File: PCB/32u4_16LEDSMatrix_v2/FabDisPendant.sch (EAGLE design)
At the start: 55 parts, among them IC1 MPR121, U1 ATMEGA32U4-AU, Y1 16MHz

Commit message: Finished PCB v2 basics
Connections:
- removed net D13: U1.PC7
- removed net D5: U1.PC6
- new net D10: U1.PB6
- new net D9: U1.PB5
- net LEDS_CI: now also U1.PC7; no longer U1.PB5
- net LEDS_DI: now also U1.PC6; no longer U1.PB6
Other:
- moved on the sheet: C20
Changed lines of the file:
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@@
 <instance part="GND35" gate="1" x="88.9" y="170.18"/>
 <instance part="R2" gate="G$1" x="154.94" y="177.8" rot="R270"/>
-<instance part="C20" gate="G$1" x="162.56" y="193.04" smashed="yes">
-<attribute name="NAME" x="161.544" y="192.913" size="1.778" layer="95" rot="R180"/>
-<attribute name="VALUE" x="161.544" y="197.739" size="1.778" layer="96" rot="R180"/>
-</instance>
-<instance part="GND37" gate="1" x="162.56" y="203.2" rot="R180"/>
+<instance part="C20" gate="G$1" x="165.1" y="193.04" smashed="yes">
+<attribute name="NAME" x="164.084" y="192.913" size="1.778" layer="95" rot="R180"/>
+<attribute name="VALUE" x="164.084" y="197.739" size="1.778" layer="96" rot="R180"/>
+</instance>
+<instance part="GND37" gate="1" x="165.1" y="203.2" rot="R180"/>
 <instance part="P+11" gate="G$1" x="154.94" y="167.64" smashed="yes" rot="R180">
 <attribute name="VALUE" x="157.226" y="164.338" size="1.778" layer="96" rot="R180"/>
@@
 <attribute name="VALUE" x="175.514" y="213.868" size="1.778" layer="96"/>
 </instance>
-<instance part="USBVCC2" gate="G$1" x="167.64" y="205.74"/>
+<instance part="USBVCC2" gate="G$1" x="168.91" y="205.74"/>
 <instance part="GND39" gate="1" x="187.96" y="139.7"/>
 <instance part="GND53" gate="1" x="241.3" y="157.48" rot="R90"/>
@@
 </segment>
 <segment>
-<wire x1="162.56" y1="200.66" x2="162.56" y2="198.12" width="0.1524" layer="91"/>
+<wire x1="165.1" y1="200.66" x2="165.1" y2="198.12" width="0.1524" layer="91"/>
 <pinref part="C20" gate="G$1" pin="1"/>
 <pinref part="GND37" gate="1" pin="GND"/>
@@
 </segment>
 <segment>
-<wire x1="60.96" y1="218.44" x2="76.2" y2="218.44" width="0.1524" layer="91"/>
-<wire x1="76.2" y1="198.12" x2="76.2" y2="218.44" width="0.1524" layer="91"/>
-<pinref part="F1" gate="G$1" pin="2"/>
-<label x="64.77" y="218.44" size="1.778" layer="95"/>
-<wire x1="101.6" y1="203.2" x2="101.6" y2="218.44" width="0.1524" layer="91"/>
-<pinref part="7803-???" gate="A1" pin="VO"/>
-<wire x1="116.84" y1="218.44" x2="101.6" y2="218.44" width="0.1524" layer="91"/>
-<pinref part="C4" gate="G$1" pin="2"/>
-<wire x1="76.2" y1="218.44" x2="101.6" y2="218.44" width="0.1524" layer="91"/>
-<junction x="76.2" y="218.44"/>
-<junction x="101.6" y="218.44"/>
-<label x="106.68" y="218.44" size="1.778" layer="95"/>
-</segment>
-<segment>
 <pinref part="ISP" gate="G$1" pin="2"/>
 <pinref part="SUPPLY2" gate="G$1" pin="VCC"/>
@@
 <label x="72.136" y="198.374" size="1.778" layer="95"/>
 <pinref part="C3" gate="G$1" pin="2"/>
+<pinref part="F1" gate="G$1" pin="2"/>
+<label x="64.77" y="218.44" size="1.778" layer="95"/>
+<wire x1="101.6" y1="203.2" x2="101.6" y2="218.44" width="0.1524" layer="91"/>
+<pinref part="7803-???" gate="A1" pin="VO"/>
+<wire x1="116.84" y1="218.44" x2="101.6" y2="218.44" width="0.1524" layer="91"/>
+<pinref part="C4" gate="G$1" pin="2"/>
+<wire x1="60.96" y1="218.44" x2="76.2" y2="218.44" width="0.1524" layer="91"/>
+<junction x="101.6" y="218.44"/>
+<label x="106.68" y="218.44" size="1.778" layer="95"/>
+<wire x1="76.2" y1="218.44" x2="101.6" y2="218.44" width="0.1524" layer="91"/>
+<wire x1="76.2" y1="198.12" x2="76.2" y2="218.44" width="0.1524" layer="91"/>
+<junction x="76.2" y="218.44"/>
 </segment>
 <segment>
@@
 <pinref part="C20" gate="G$1" pin="2"/>
 <pinref part="U1" gate="A" pin="AREF"/>
-<wire x1="162.56" y1="190.5" x2="190.5" y2="190.5" width="0.1524" layer="91"/>
+<wire x1="165.1" y1="190.5" x2="190.5" y2="190.5" width="0.1524" layer="91"/>
 </segment>
 </net>
@@
 <wire x1="190.5" y1="187.96" x2="162.56" y2="187.96" width="0.1524" layer="91"/>
 <junction x="162.56" y="187.96"/>
+<label x="154.94" y="187.96" size="1.778" layer="95"/>
 </segment>
 <segment>
@@
 <wire x1="226.06" y1="170.18" x2="236.22" y2="170.18" width="0.1524" layer="91"/>
 <label x="231.14" y="170.18" size="1.778" layer="95"/>
-</segment>
-</net>
-<net name="D5" class="0">
-<segment>
-<pinref part="U1" gate="A" pin="PC6"/>
-<wire x1="226.06" y1="187.96" x2="236.22" y2="187.96" width="0.1524" layer="91"/>
-<label x="231.14" y="187.96" size="1.778" layer="95"/>
 </segment>
 </net>
@@
 <pinref part="U1" gate="A" pin="UVCC"/>
 <wire x1="190.5" y1="205.74" x2="185.42" y2="205.74" width="0.1524" layer="91"/>
-<wire x1="185.42" y1="205.74" x2="167.64" y2="205.74" width="0.1524" layer="91"/>
+<wire x1="185.42" y1="205.74" x2="168.91" y2="205.74" width="0.1524" layer="91"/>
 <wire x1="185.42" y1="180.34" x2="185.42" y2="205.74" width="0.1524" layer="91"/>
 <pinref part="USBVCC2" gate="G$1" pin="3.3V"/>
@@
 <wire x1="226.06" y1="165.1" x2="236.22" y2="165.1" width="0.1524" layer="91"/>
 <label x="231.14" y="165.1" size="1.778" layer="95"/>
-</segment>
-</net>
-<net name="D13" class="0">
-<segment>
-<pinref part="U1" gate="A" pin="PC7"/>
-<wire x1="226.06" y1="185.42" x2="236.22" y2="185.42" width="0.1524" layer="91"/>
-<label x="231.14" y="185.42" size="1.778" layer="95"/>
 </segment>
 </net>
@@
 </segment>
 <segment>
-<pinref part="U1" gate="A" pin="PB6"/>
-<wire x1="226.06" y1="195.58" x2="236.22" y2="195.58" width="0.1524" layer="91"/>
-<label x="231.14" y="195.58" size="1.778" layer="95"/>
+<pinref part="U1" gate="A" pin="PC6"/>
+<wire x1="226.06" y1="187.96" x2="236.22" y2="187.96" width="0.1524" layer="91"/>
+<label x="231.14" y="187.96" size="1.778" layer="95"/>
 </segment>
 </net>
@@
 </segment>
 <segment>
-<pinref part="U1" gate="A" pin="PB5"/>
-<wire x1="226.06" y1="198.12" x2="236.22" y2="198.12" width="0.1524" layer="91"/>
-<label x="231.14" y="198.12" size="1.778" layer="95"/>
+<pinref part="U1" gate="A" pin="PC7"/>
+<wire x1="226.06" y1="185.42" x2="236.22" y2="185.42" width="0.1524" layer="91"/>
+<label x="231.14" y="185.42" size="1.778" layer="95"/>
 </segment>
 </net>
@@
 </segment>
 </net>
+<net name="D9" class="0">
+<segment>
+<pinref part="U1" gate="A" pin="PB5"/>
+<wire x1="226.06" y1="198.12" x2="236.22" y2="198.12" width="0.1524" layer="91"/>
+<label x="231.14" y="198.12" size="1.778" layer="95"/>
+</segment>
+</net>
+<net name="D10" class="0">
+<segment>
+<pinref part="U1" gate="A" pin="PB6"/>
+<wire x1="226.06" y1="195.58" x2="236.22" y2="195.58" width="0.1524" layer="91"/>
+<label x="231.14" y="195.58" size="1.778" layer="95"/>
+</segment>
+</net>

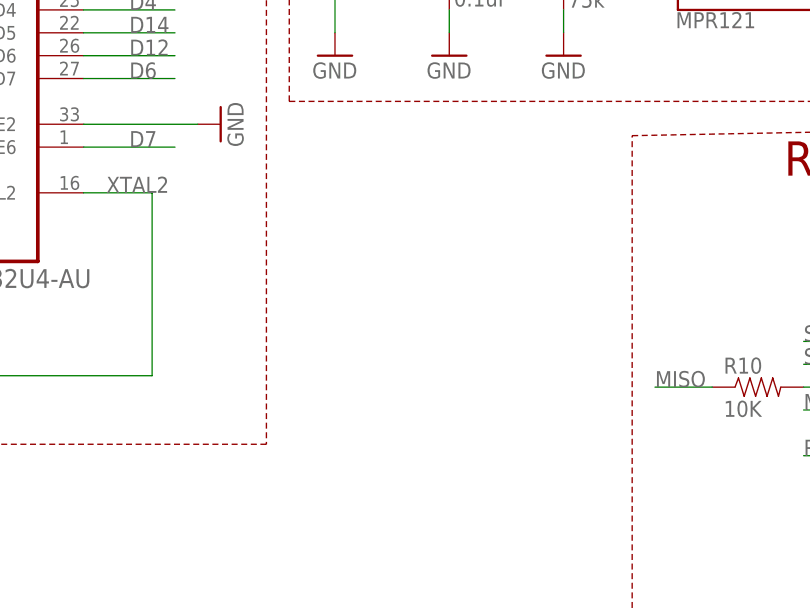
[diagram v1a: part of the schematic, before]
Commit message: Added headers for some digital and analog pins
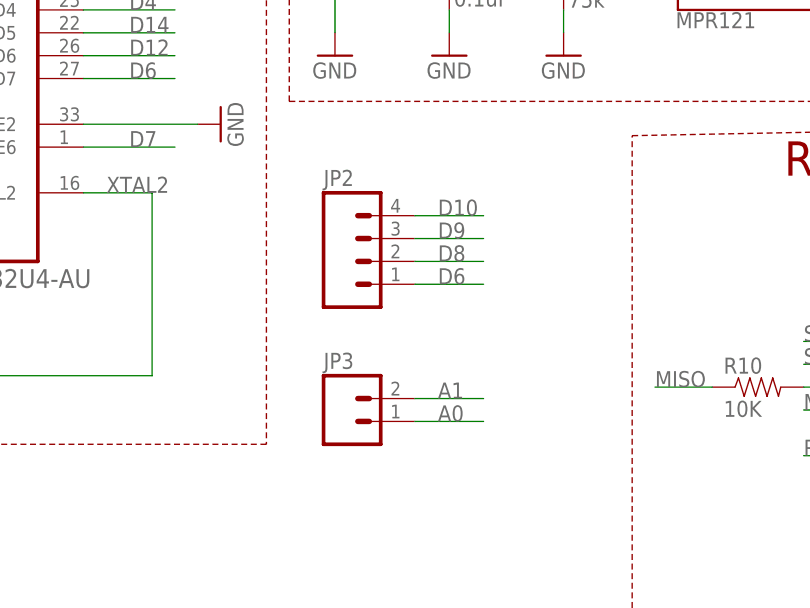
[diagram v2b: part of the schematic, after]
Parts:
- added JP2: (no value), SparkFun-Connectors:M04PTH
- added JP3: (no value), SparkFun-Connectors:M02PTH
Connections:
- net A0: now also JP3.1
- net A1: now also JP3.2
- net D10: now also JP2.4
- net D6: now also JP2.1
- net D8: now also JP2.2
- net D9: now also JP2.3
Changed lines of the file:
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@@
 <part name="PWRSWITCH" library="SparkFun" deviceset="SWITCH-MOMENTARY-2" device="SMD" value="Reset"/>
 <part name="JP1" library="SparkFun-Connectors" deviceset="M02" device="PTH"/>
+<part name="JP2" library="SparkFun-Connectors" deviceset="M04" device="PTH"/>
+<part name="JP3" library="SparkFun-Connectors" deviceset="M02" device="PTH"/>
 </parts>
 <sheets>
@@
 <instance part="PWRSWITCH" gate="G$1" x="55.88" y="166.37" rot="R180"/>
 <instance part="JP1" gate="G$1" x="314.96" y="245.11" rot="R180"/>
+<instance part="JP2" gate="G$1" x="257.81" y="142.24"/>
+<instance part="JP3" gate="G$1" x="255.27" y="124.46"/>
 </instances>
 <busses>
@@
 <label x="231.14" y="200.66" size="1.778" layer="95"/>
 </segment>
+<segment>
+<pinref part="JP2" gate="G$1" pin="2"/>
+<wire x1="262.89" y1="142.24" x2="270.51" y2="142.24" width="0.1524" layer="91"/>
+<label x="265.43" y="142.24" size="1.778" layer="95"/>
+</segment>
 </net>
 <net name="A5" class="0">
@@
 <label x="180.34" y="165.1" size="1.778" layer="95"/>
 </segment>
+<segment>
+<pinref part="JP3" gate="G$1" pin="2"/>
+<wire x1="262.89" y1="127" x2="270.51" y2="127" width="0.1524" layer="91"/>
+<label x="265.43" y="127" size="1.778" layer="95"/>
+</segment>
 </net>
 <net name="D4" class="0">
@@
 <wire x1="226.06" y1="162.56" x2="236.22" y2="162.56" width="0.1524" layer="91"/>
 <label x="231.14" y="162.56" size="1.778" layer="95"/>
+</segment>
+<segment>
+<pinref part="JP2" gate="G$1" pin="1"/>
+<wire x1="262.89" y1="139.7" x2="270.51" y2="139.7" width="0.1524" layer="91"/>
+<label x="265.43" y="139.7" size="1.778" layer="95"/>
 </segment>
 </net>
@@
 <label x="180.34" y="162.56" size="1.778" layer="95"/>
 </segment>
+<segment>
+<pinref part="JP3" gate="G$1" pin="1"/>
+<wire x1="262.89" y1="124.46" x2="270.51" y2="124.46" width="0.1524" layer="91"/>
+<label x="265.43" y="124.46" size="1.778" layer="95"/>
+</segment>
 </net>
 <net name="N$1" class="0">
@@
 <label x="231.14" y="198.12" size="1.778" layer="95"/>
 </segment>
+<segment>
+<pinref part="JP2" gate="G$1" pin="3"/>
+<wire x1="262.89" y1="144.78" x2="270.51" y2="144.78" width="0.1524" layer="91"/>
+<label x="265.43" y="144.78" size="1.778" layer="95"/>
+</segment>
 </net>
 <net name="D10" class="0">
@@
 <label x="231.14" y="195.58" size="1.778" layer="95"/>
 </segment>
-</net>
+<segment>
+<pinref part="JP2" gate="G$1" pin="4"/>
+<wire x1="262.89" y1="147.32" x2="270.51" y2="147.32" width="0.1524" layer="91"/>
+<label x="265.43" y="147.32" size="1.778" layer="95"/>
+</segment>
+</net>

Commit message: FInished up changes to the board
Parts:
- removed PWRSWITCH: Reset, SparkFun:SWITCH-MOMENTARY-2SMD
- added D2: (no value), SparkFun:DIODESOD
- added R12: 10k, SparkFun:RESISTOR0603-RES
- added SWITCH: SWITCH, SparkFun-Connectors:M03X2FEMALE
- R10: value 10K -> 4.7k
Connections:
- removed net D10: JP2.4, U1.PB6
- removed net D9: JP2.3, U1.PB5
- new net D13: JP2.4, U1.PC7
- new net D5: JP2.3, U1.PC6
- new net N$37: 7803-???.VO, C4.2, D2.C
- net 3.3V: now also R12.2
- net 5V: now also D2.A; no longer 7803-???.VO, C4.2
- net LEDS_CI: now also U1.PB6; no longer U1.PC7
- net LEDS_DI: now also U1.PB5; no longer U1.PC6
- net N$36: now also SWITCH.6; no longer PWRSWITCH.1
- net RAW: now also SWITCH.4; no longer PWRSWITCH.2
- net SS: now also R12.1
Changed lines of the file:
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@@
 <part name="GND16" library="SparkFun-Aesthetics" deviceset="GND" device=""/>
 <part name="LED15" library="APA102" deviceset="APA102" device=""/>
-<part name="R10" library="SparkFun" deviceset="RESISTOR" device="0603-RES" value="10K"/>
+<part name="R10" library="SparkFun" deviceset="RESISTOR" device="0603-RES" value="4.7k"/>
 <part name="C1" library="SparkFun-Capacitors" deviceset="10UF-6.3V-20%(1206)" device="" value="10uF"/>
 <part name="C2" library="SparkFun-Capacitors" deviceset="10UF-6.3V-20%(1206)" device="" value="10uF"/>
@@
 <part name="C4" library="SparkFun-Capacitors" deviceset="10UF-6.3V-20%(1206)" device="" value="10uF"/>
 <part name="C5" library="SparkFun-Capacitors" deviceset="10UF-6.3V-20%(1206)" device="" value="1uF"/>
-<part name="PWRSWITCH" library="SparkFun" deviceset="SWITCH-MOMENTARY-2" device="SMD" value="Reset"/>
 <part name="JP1" library="SparkFun-Connectors" deviceset="M02" device="PTH"/>
 <part name="JP2" library="SparkFun-Connectors" deviceset="M04" device="PTH"/>
 <part name="JP3" library="SparkFun-Connectors" deviceset="M02" device="PTH"/>
+<part name="D2" library="SparkFun" deviceset="DIODE" device="SOD"/>
+<part name="R12" library="SparkFun" deviceset="RESISTOR" device="0603-RES" value="10k"/>
+<part name="SWITCH" library="SparkFun-Connectors" deviceset="M03X2" device="FEMALE" value="SWITCH"/>
 </parts>
 <sheets>
@@
 <wire x1="353.06" y1="101.6" x2="287.02" y2="101.6" width="0.1524" layer="94" style="shortdash"/>
 <wire x1="287.02" y1="101.6" x2="287.02" y2="156.21" width="0.1524" layer="94" style="shortdash"/>
-<text x="303.911" y="151.765" size="3.81" layer="94">Radio</text>
 <wire x1="248.92" y1="223.52" x2="353.06" y2="223.52" width="0.1524" layer="94" style="shortdash"/>
 <wire x1="353.06" y1="223.52" x2="353.06" y2="160.02" width="0.1524" layer="94" style="shortdash"/>
@@
 <wire x1="142.24" y1="121.92" x2="142.24" y2="223.52" width="0.1524" layer="94" style="shortdash"/>
 <text x="143.891" y="217.805" size="3.81" layer="94">ATMEGA 32u4</text>
+<text x="288.671" y="150.495" size="3.81" layer="94">Radio</text>
 </plain>
 <instances>
@@
 <instance part="GND45" gate="1" x="91.44" y="116.84"/>
 <instance part="SUPPLY18" gate="GND" x="334.01" y="110.49"/>
-<instance part="P+3" gate="1" x="334.01" y="144.78"/>
+<instance part="P+3" gate="1" x="334.01" y="149.86"/>
 <instance part="U$1" gate="G$1" x="346.71" y="146.05" rot="R90"/>
 <instance part="RMF69" gate="G$1" x="334.01" y="125.73"/>
@@
 <instance part="C4" gate="G$1" x="101.6" y="200.66" rot="R180"/>
 <instance part="C5" gate="G$1" x="132.08" y="200.66" rot="R180"/>
-<instance part="PWRSWITCH" gate="G$1" x="55.88" y="166.37" rot="R180"/>
 <instance part="JP1" gate="G$1" x="314.96" y="245.11" rot="R180"/>
 <instance part="JP2" gate="G$1" x="257.81" y="142.24"/>
 <instance part="JP3" gate="G$1" x="255.27" y="124.46"/>
+<instance part="D2" gate="G$1" x="88.9" y="218.44"/>
+<instance part="R12" gate="G$1" x="313.69" y="140.97" smashed="yes" rot="R90">
+<attribute name="NAME" x="317.754" y="145.8214" size="1.778" layer="95" rot="R180"/>
+<attribute name="VALUE" x="312.166" y="138.938" size="1.778" layer="96" rot="R90"/>
+</instance>
+<instance part="SWITCH" gate="G$1" x="46.99" y="168.91"/>
 </instances>
 <busses>
@@
 <pinref part="F1" gate="G$1" pin="2"/>
 <label x="64.77" y="218.44" size="1.778" layer="95"/>
-<wire x1="101.6" y1="203.2" x2="101.6" y2="218.44" width="0.1524" layer="91"/>
-<pinref part="7803-???" gate="A1" pin="VO"/>
-<wire x1="116.84" y1="218.44" x2="101.6" y2="218.44" width="0.1524" layer="91"/>
-<pinref part="C4" gate="G$1" pin="2"/>
 <wire x1="60.96" y1="218.44" x2="76.2" y2="218.44" width="0.1524" layer="91"/>
-<junction x="101.6" y="218.44"/>
-<label x="106.68" y="218.44" size="1.778" layer="95"/>
-<wire x1="76.2" y1="218.44" x2="101.6" y2="218.44" width="0.1524" layer="91"/>
 <wire x1="76.2" y1="198.12" x2="76.2" y2="218.44" width="0.1524" layer="91"/>
+<pinref part="D2" gate="G$1" pin="A"/>
+<wire x1="86.36" y1="218.44" x2="76.2" y2="218.44" width="0.1524" layer="91"/>
 <junction x="76.2" y="218.44"/>
 </segment>
@@
 <net name="RAW" class="1">
 <segment>
-<pinref part="PWRSWITCH" gate="G$1" pin="2"/>
-<wire x1="50.8" y1="166.37" x2="43.18" y2="166.37" width="0.1524" layer="91"/>
-<label x="43.18" y="166.37" size="1.778" layer="95"/>
-</segment>
-<segment>
 <wire x1="45.72" y1="198.12" x2="35.56" y2="198.12" width="0.1524" layer="91"/>
 <wire x1="50.8" y1="198.12" x2="45.72" y2="198.12" width="0.1524" layer="91"/>
@@
 <pinref part="C2" gate="G$1" pin="2"/>
 <label x="35.56" y="198.12" size="1.778" layer="95"/>
+</segment>
+<segment>
+<pinref part="SWITCH" gate="G$1" pin="4"/>
+<wire x1="54.61" y1="168.91" x2="62.23" y2="168.91" width="0.1524" layer="91"/>
 </segment>
 </net>
@@
 </segment>
 <segment>
-<pinref part="U1" gate="A" pin="PC6"/>
-<wire x1="226.06" y1="187.96" x2="236.22" y2="187.96" width="0.1524" layer="91"/>
-<label x="231.14" y="187.96" size="1.778" layer="95"/>
+<pinref part="U1" gate="A" pin="PB5"/>
+<wire x1="226.06" y1="198.12" x2="236.22" y2="198.12" width="0.1524" layer="91"/>
+<label x="231.14" y="198.12" size="1.778" layer="95"/>
 </segment>
 </net>
 <net name="SS" class="0">
 <segment>
-<wire x1="306.07" y1="133.35" x2="321.31" y2="133.35" width="0.1524" layer="91"/>
+<wire x1="306.07" y1="133.35" x2="313.69" y2="133.35" width="0.1524" layer="91"/>
 <label x="306.07" y="133.35" size="1.778" layer="95"/>
 <pinref part="RMF69" gate="G$1" pin="SEL"/>
+<pinref part="R12" gate="G$1" pin="1"/>
+<wire x1="313.69" y1="133.35" x2="321.31" y2="133.35" width="0.1524" layer="91"/>
+<wire x1="313.69" y1="135.89" x2="313.69" y2="133.35" width="0.1524" layer="91"/>
+<junction x="313.69" y="133.35"/>
 </segment>
 <segment>
@@
 <segment>
 <pinref part="P+3" gate="1" pin="VCC"/>
-<wire x1="334.01" y1="144.78" x2="334.01" y2="140.97" width="0.1524" layer="91"/>
+<wire x1="334.01" y1="149.86" x2="334.01" y2="147.32" width="0.1524" layer="91"/>
 <pinref part="RMF69" gate="G$1" pin="VCC"/>
+<pinref part="R12" gate="G$1" pin="2"/>
+<wire x1="334.01" y1="147.32" x2="334.01" y2="140.97" width="0.1524" layer="91"/>
+<wire x1="313.69" y1="146.05" x2="313.69" y2="147.32" width="0.1524" layer="91"/>
+<wire x1="313.69" y1="147.32" x2="334.01" y2="147.32" width="0.1524" layer="91"/>
+<junction x="334.01" y="147.32"/>
 </segment>
 <segment>
@@
 </segment>
 <segment>
-<pinref part="U1" gate="A" pin="PC7"/>
-<wire x1="226.06" y1="185.42" x2="236.22" y2="185.42" width="0.1524" layer="91"/>
-<label x="231.14" y="185.42" size="1.778" layer="95"/>
+<pinref part="U1" gate="A" pin="PB6"/>
+<wire x1="226.06" y1="195.58" x2="236.22" y2="195.58" width="0.1524" layer="91"/>
+<label x="231.14" y="195.58" size="1.778" layer="95"/>
 </segment>
 </net>
@@
 <segment>
 <pinref part="PWR" gate="G$1" pin="1"/>
-<pinref part="PWRSWITCH" gate="G$1" pin="1"/>
-<wire x1="60.96" y1="166.37" x2="63.5" y2="166.37" width="0.1524" layer="91"/>
-</segment>
-</net>
-<net name="D9" class="0">
-<segment>
-<pinref part="U1" gate="A" pin="PB5"/>
-<wire x1="226.06" y1="198.12" x2="236.22" y2="198.12" width="0.1524" layer="91"/>
-<label x="231.14" y="198.12" size="1.778" layer="95"/>
+<wire x1="54.61" y1="166.37" x2="63.5" y2="166.37" width="0.1524" layer="91"/>
+<pinref part="SWITCH" gate="G$1" pin="6"/>
+</segment>
+</net>
+<net name="N$37" class="0">
+<segment>
+<pinref part="7803-???" gate="A1" pin="VO"/>
+<wire x1="116.84" y1="218.44" x2="101.6" y2="218.44" width="0.1524" layer="91"/>
+<wire x1="101.6" y1="203.2" x2="101.6" y2="218.44" width="0.1524" layer="91"/>
+<pinref part="C4" gate="G$1" pin="2"/>
+<label x="106.68" y="218.44" size="1.778" layer="95"/>
+<pinref part="D2" gate="G$1" pin="C"/>
+<wire x1="91.44" y1="218.44" x2="101.6" y2="218.44" width="0.1524" layer="91"/>
+<junction x="101.6" y="218.44"/>
+</segment>
+</net>
+<net name="D5" class="0">
+<segment>
+<pinref part="U1" gate="A" pin="PC6"/>
+<wire x1="226.06" y1="187.96" x2="236.22" y2="187.96" width="0.1524" layer="91"/>
+<label x="231.14" y="187.96" size="1.778" layer="95"/>
 </segment>
 <segment>
@@
 </segment>
 </net>
-<net name="D10" class="0">
-<segment>
-<pinref part="U1" gate="A" pin="PB6"/>
-<wire x1="226.06" y1="195.58" x2="236.22" y2="195.58" width="0.1524" layer="91"/>
-<label x="231.14" y="195.58" size="1.778" layer="95"/>
-</segment>
-<segment>
+<net name="D13" class="0">
+<segment>
+<pinref part="U1" gate="A" pin="PC7"/>
+<wire x1="226.06" y1="185.42" x2="236.22" y2="185.42" width="0.1524" layer="91"/>
+<label x="231.14" y="185.42" size="1.778" layer="95"/>
+</segment>
+<segment>
